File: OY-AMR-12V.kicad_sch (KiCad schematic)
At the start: 20 parts

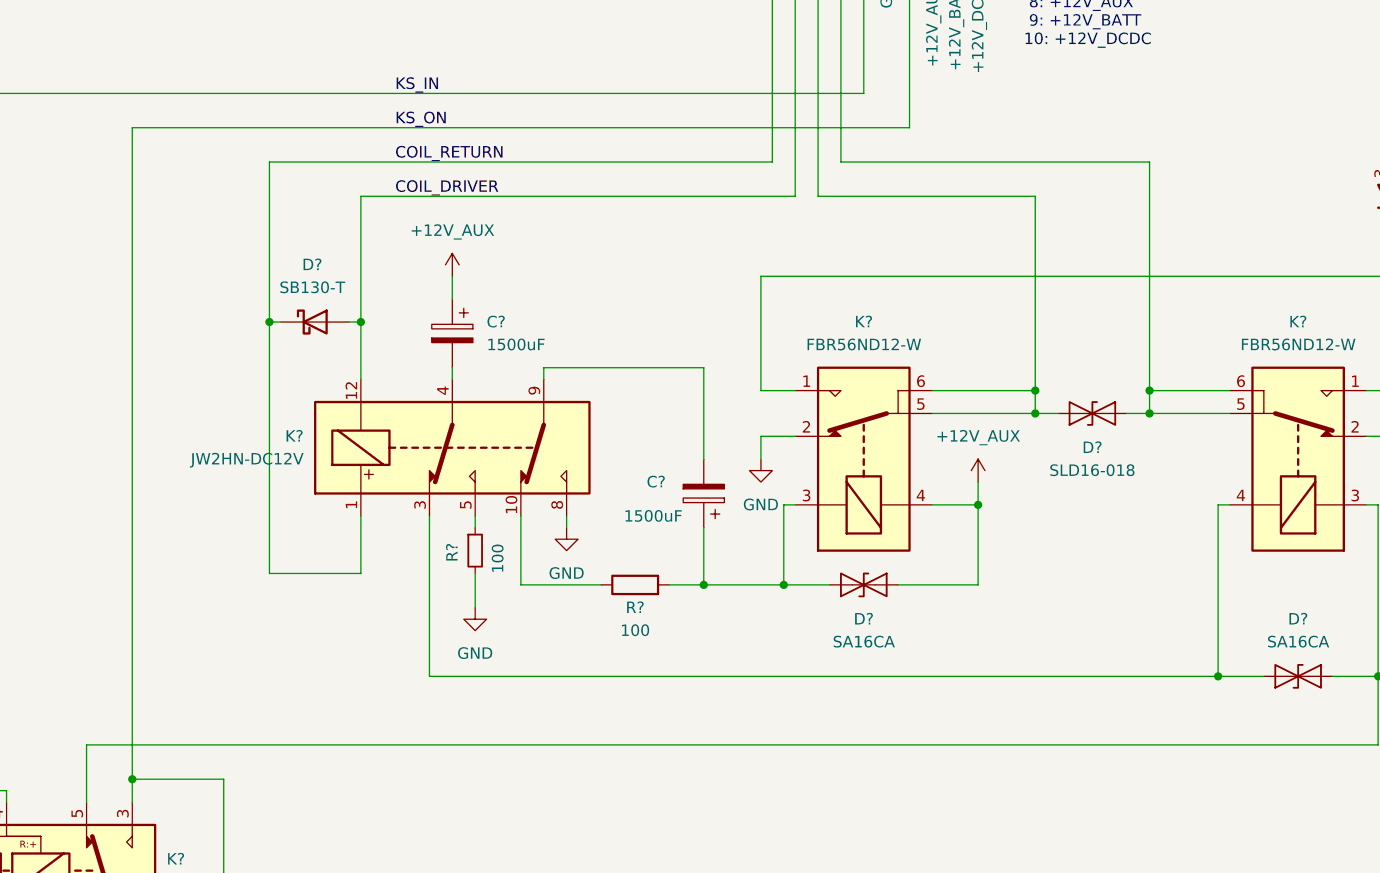
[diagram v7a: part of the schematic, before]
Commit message: Updated DPDT relay to 2xSPDT automotive relays
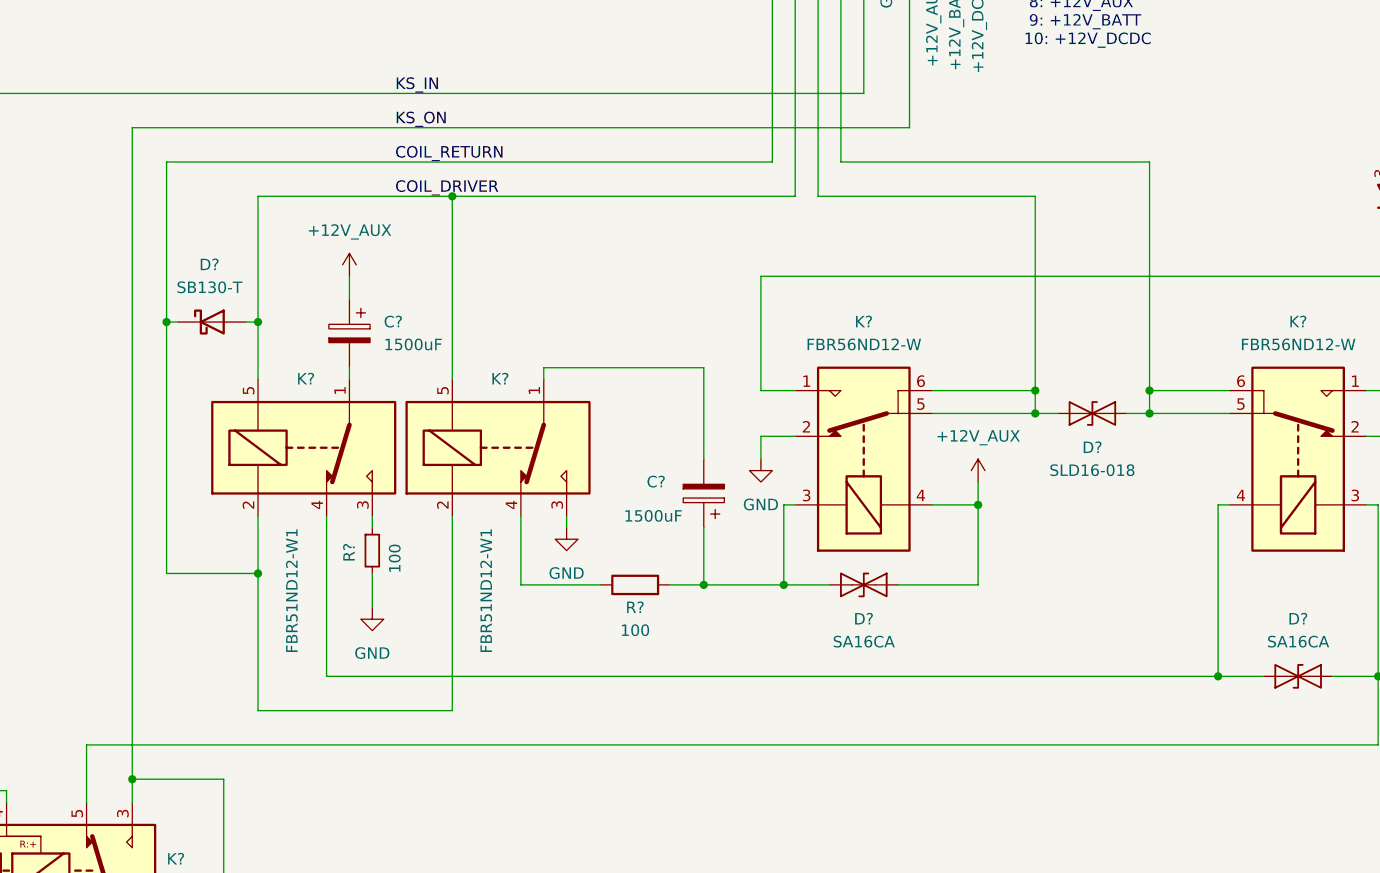
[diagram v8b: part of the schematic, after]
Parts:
- removed K?: JW2HN-DC12V, Relay_THT:Relay_DPDT_Kemet_EC2, symbol Relay:EC2-3NU
- added K? (x2): FBR51ND12-W1, Relay_THT:Relay_SPDT_Omron_G6E, symbol Miscellaneous:FBR51ND12-W1
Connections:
- net COIL_DRIVER: now also K?.5, K?.5
- net COIL_RETURN: now also K?.2, K?.2
- net GND: now also K?.3
- net at C?.2: now also K?.1 (x2)
- net at R?.1: now also K?.3
- net at D?.1 (A1), K?.4: now also K?.4
- net at R?.1: now also K?.4
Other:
- moved on the sheet: C?, D?, R?
